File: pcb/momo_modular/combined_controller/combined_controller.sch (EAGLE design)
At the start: 44 parts, among them Q2 P-MOSFET, U1 XRP7659, U2 PIC24FJ64GA306, U3 MCP1702, U5 FLASH8MSOP8, U6 MCP73811

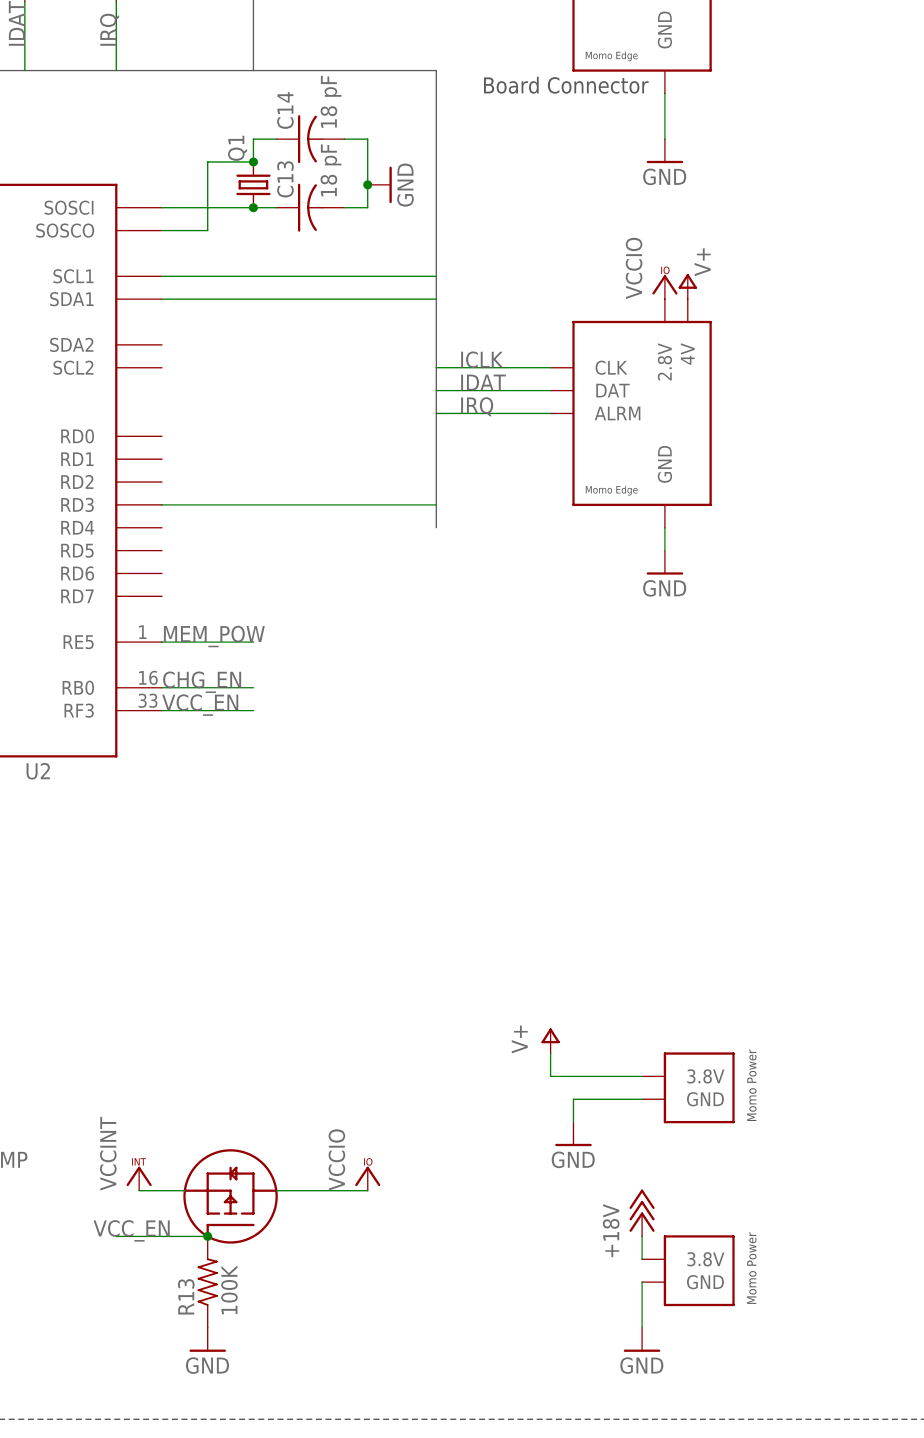
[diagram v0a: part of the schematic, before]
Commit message: Finalize combined controller layout
- Switch power connector to one that doesn't require a board cutout
- Relay out traces better given that we note have more space
- Make the board a regular shape
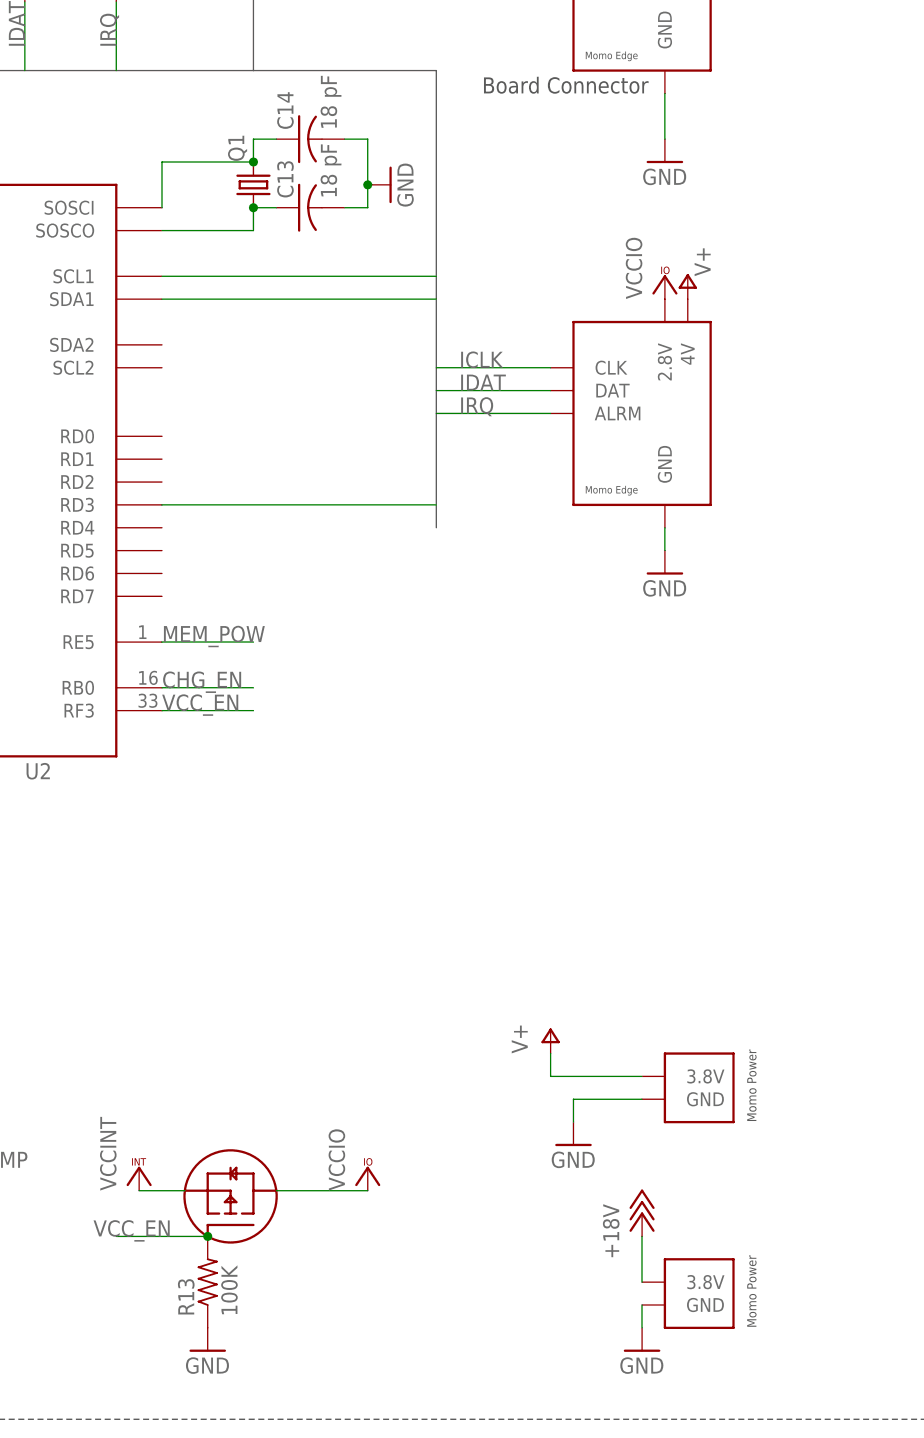
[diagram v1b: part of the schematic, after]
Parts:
- JP4, JP5: value MOMO-EDGE-POWER-M -> MOMO-PWR-HOUSED; device components:MOMO-EDGE-POWER-M -> components:MOMO-PWR-HOUSED; DIGIKEY-PN A19450-ND -> (none)
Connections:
- net +18V: now also JP4.3.8V; no longer JP5.3.8V
- net N$6: now also U2.SOSCI; no longer U2.SOSCO
- net N$7: now also U2.SOSCO; no longer U2.SOSCI
- net V+: now also JP5.3.8V; no longer JP4.3.8V
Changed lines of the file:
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@@
 <?xml version="1.0" encoding="utf-8"?>
 <!DOCTYPE eagle SYSTEM "eagle.dtd">
-<eagle version="6.4">
+<eagle version="6.5.0">
 <drawing>
 <settings>
@@
 <attribute name="DIGIKEY-PN-SOLAR" value="P0.0GCT-ND"/>
 </part>
-<part name="JP5" library="components" deviceset="MOMO-EDGE-POWER-M" device="">
-<attribute name="DIGIKEY-PN" value="A19450-ND"/>
-</part>
-<part name="JP4" library="components" deviceset="MOMO-EDGE-POWER-M" device="">
-<attribute name="DIGIKEY-PN" value="A19450-ND"/>
-</part>
 <part name="VCC2" library="supply1" deviceset="VCCIO" device=""/>
 <part name="VCC11" library="supply1" deviceset="VCCIO" device=""/>
@@
 <attribute name="DIGIKEY-PN" value="445-1265-1-ND"/>
 </part>
+<part name="JP4" library="components" deviceset="MOMO-PWR-HOUSED" device=""/>
+<part name="JP5" library="components" deviceset="MOMO-PWR-HOUSED" device=""/>
 </parts>
 <sheets>
@@
 <attribute name="DIGIKEY-PN-SOLAR" x="-180.34" y="116.84" size="1.778" layer="96" display="off"/>
 </instance>
-<instance part="JP5" gate="G$1" x="-30.48" y="-96.52">
-<attribute name="DIGIKEY-PN" x="-30.48" y="-96.52" size="1.778" layer="96" display="off"/>
-</instance>
-<instance part="JP4" gate="G$1" x="-30.48" y="-76.2">
-<attribute name="DIGIKEY-PN" x="-30.48" y="-76.2" size="1.778" layer="96" display="off"/>
-</instance>
 <instance part="VCC2" gate="G$1" x="-30.48" y="15.24"/>
 <instance part="VCC11" gate="G$1" x="-30.48" y="63.5"/>
@@
 <attribute name="DIGIKEY-PN" x="-205.74" y="68.58" size="1.778" layer="96" display="off"/>
 </instance>
+<instance part="JP4" gate="G$1" x="-30.48" y="-99.06"/>
+<instance part="JP5" gate="G$1" x="-30.48" y="-76.2"/>
 </instances>
 <busses>
@@
 </segment>
 <segment>
-<pinref part="GND7" gate="1" pin="GND"/>
-<pinref part="JP5" gate="G$1" pin="GND"/>
-<wire x1="-33.02" y1="-101.6" x2="-33.02" y2="-96.52" width="0.1524" layer="91"/>
-</segment>
-<segment>
-<pinref part="JP4" gate="G$1" pin="GND"/>
 <pinref part="GND8" gate="1" pin="GND"/>
 <wire x1="-33.02" y1="-76.2" x2="-40.64" y2="-76.2" width="0.1524" layer="91"/>
 <wire x1="-40.64" y1="-76.2" x2="-40.64" y2="-78.74" width="0.1524" layer="91"/>
+<pinref part="JP5" gate="G$1" pin="GND"/>
 </segment>
 <segment>
@@
 <pinref part="GND6" gate="1" pin="GND"/>
 </segment>
+<segment>
+<pinref part="GND7" gate="1" pin="GND"/>
+<wire x1="-33.02" y1="-99.06" x2="-33.02" y2="-101.6" width="0.1524" layer="91"/>
+<pinref part="JP4" gate="G$1" pin="GND"/>
+</segment>
 </net>
 <net name="V+" class="0">
@@
 <wire x1="-33.02" y1="-73.66" x2="-43.18" y2="-73.66" width="0.1524" layer="91"/>
 <wire x1="-43.18" y1="-73.66" x2="-43.18" y2="-71.12" width="0.1524" layer="91"/>
-<pinref part="JP4" gate="G$1" pin="3.8V"/>
+<pinref part="JP5" gate="G$1" pin="3.8V"/>
 </segment>
 </net>
@@
 </segment>
 <segment>
-<pinref part="JP5" gate="G$1" pin="3.8V"/>
 <pinref part="P+5" gate="1" pin="+18V"/>
-<wire x1="-33.02" y1="-93.98" x2="-33.02" y2="-91.44" width="0.1524" layer="91"/>
+<wire x1="-33.02" y1="-96.52" x2="-33.02" y2="-91.44" width="0.1524" layer="91"/>
+<pinref part="JP4" gate="G$1" pin="3.8V"/>
 </segment>
 </net>
@@
 <wire x1="-76.2" y1="27.94" x2="-76.2" y2="30.48" width="0.1524" layer="91"/>
 <wire x1="-76.2" y1="30.48" x2="-73.66" y2="30.48" width="0.1524" layer="91"/>
-<pinref part="U2" gate="G$1" pin="SOSCO"/>
-<wire x1="-86.36" y1="20.32" x2="-81.28" y2="20.32" width="0.1524" layer="91"/>
-<wire x1="-81.28" y1="20.32" x2="-81.28" y2="27.94" width="0.1524" layer="91"/>
-<wire x1="-81.28" y1="27.94" x2="-76.2" y2="27.94" width="0.1524" layer="91"/>
 <junction x="-76.2" y="27.94"/>
+<pinref part="U2" gate="G$1" pin="SOSCI"/>
+<wire x1="-86.36" y1="22.86" x2="-86.36" y2="27.94" width="0.1524" layer="91"/>
+<wire x1="-86.36" y1="27.94" x2="-76.2" y2="27.94" width="0.1524" layer="91"/>
 </segment>
 </net>
@@
 <pinref part="C13" gate="G$1" pin="1"/>
 <wire x1="-73.66" y1="22.86" x2="-76.2" y2="22.86" width="0.1524" layer="91"/>
-<pinref part="U2" gate="G$1" pin="SOSCI"/>
-<wire x1="-86.36" y1="22.86" x2="-76.2" y2="22.86" width="0.1524" layer="91"/>
+<wire x1="-76.2" y1="22.86" x2="-76.2" y2="20.32" width="0.1524" layer="91"/>
 <junction x="-76.2" y="22.86"/>
-</segment>
-</net>
+<pinref part="U2" gate="G$1" pin="SOSCO"/>
+<wire x1="-76.2" y1="20.32" x2="-86.36" y2="20.32" width="0.1524" layer="91"/>
+</segment>
+</net>

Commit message: Final review of combined controller
- checked footprint of uc
- added bypass for battery if required
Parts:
- added R12: 0R, rcl:R-US_R0603
- C15: DIGIKEY-PN 1276-1119-1-ND -> 1276-2893-1-ND
- JP3: POPULATE (none) -> no
- Q1: value (none) -> 32.768khz
- Q2: DESCRIPTION (none) -> P Channel MOSFET
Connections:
- net VBAT: now also R12.2
- net VCCINT: now also R12.1
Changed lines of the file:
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@@
 <part name="VCC2" library="supply1" deviceset="VCCIO" device=""/>
 <part name="VCC11" library="supply1" deviceset="VCCIO" device=""/>
-<part name="Q2" library="components" deviceset="P-MOSFET" device=""/>
+<part name="Q2" library="components" deviceset="P-MOSFET" device="">
+<attribute name="DESCRIPTION" value="P Channel MOSFET"/>
+</part>
 <part name="R13" library="rcl" deviceset="R-US_" device="R0603" value="100K">
 <attribute name="DIGIKEY-PN" value="P100KHCT-ND"/>
@@
 <attribute name="DIGIKEY-PN" value="S1011EC-06-ND"/>
 </part>
-<part name="JP3" library="pinhead" deviceset="PINHD-1X1" device=""/>
+<part name="JP3" library="pinhead" deviceset="PINHD-1X1" device="">
+<attribute name="DIGIKEY-PN" value=""/>
+<attribute name="POPULATE" value="no"/>
+</part>
 <part name="D2" library="diode" deviceset="DIODE-" device="DO214AC">
 <attribute name="DESCRIPTION" value="Schottky Diode "/>
@@
 <attribute name="DIGIKEY-PN-SOLAR" value="MCP73811T-420I/OTCT-ND"/>
 </part>
-<part name="Q1" library="crystal" deviceset="CRYSTAL" device="TC26H">
+<part name="Q1" library="crystal" deviceset="CRYSTAL" device="TC26H" value="32.768khz">
 <attribute name="DIGIKEY-PN" value="535-9034-ND"/>
 </part>
@@
 <part name="GND5" library="supply1" deviceset="GND" device=""/>
 <part name="C15" library="rcl" deviceset="C-US" device="C0805" value="10 uF">
-<attribute name="DIGIKEY-PN" value="1276-1119-1-ND"/>
+<attribute name="DIGIKEY-PN" value="1276-2893-1-ND"/>
 </part>
 <part name="GND6" library="supply1" deviceset="GND" device=""/>
@@
 <part name="JP4" library="components" deviceset="MOMO-PWR-HOUSED" device=""/>
 <part name="JP5" library="components" deviceset="MOMO-PWR-HOUSED" device=""/>
+<part name="R12" library="rcl" deviceset="R-US_" device="R0603" value="0R">
+<attribute name="DIGIKEY-PN" value="P0.0GCT-ND"/>
+<attribute name="POPULATE" value="no"/>
+</part>
+<part name="VCC12" library="supply1" deviceset="VCCINT" device=""/>
 </parts>
 <sheets>
 <sheet>
 <plain>
-<wire x1="-226.06" y1="127" x2="-226.06" y2="-111.76" width="0.1524" layer="97" style="longdash"/>
-<wire x1="-226.06" y1="-111.76" x2="10.16" y2="-111.76" width="0.1524" layer="97" style="longdash"/>
+<wire x1="-238.76" y1="127" x2="-238.76" y2="-111.76" width="0.1524" layer="97" style="longdash"/>
+<wire x1="-238.76" y1="-111.76" x2="10.16" y2="-111.76" width="0.1524" layer="97" style="longdash"/>
 <wire x1="10.16" y1="-111.76" x2="10.16" y2="127" width="0.1524" layer="97" style="longdash"/>
-<wire x1="10.16" y1="127" x2="-226.06" y2="127" width="0.1524" layer="97" style="longdash"/>
+<wire x1="10.16" y1="127" x2="-238.76" y2="127" width="0.1524" layer="97" style="longdash"/>
 <wire x1="-223.52" y1="-109.22" x2="-223.52" y2="-96.52" width="0.3048" layer="97"/>
 <wire x1="-223.52" y1="-96.52" x2="-223.52" y2="-91.44" width="0.3048" layer="97"/>
@@
 <instance part="VCC2" gate="G$1" x="-30.48" y="15.24"/>
 <instance part="VCC11" gate="G$1" x="-30.48" y="63.5"/>
-<instance part="Q2" gate="G$1" x="-78.74" y="-86.36" rot="R90"/>
+<instance part="Q2" gate="G$1" x="-78.74" y="-86.36" rot="R90">
+<attribute name="DESCRIPTION" x="-78.74" y="-86.36" size="1.778" layer="96" rot="R90" display="off"/>
+</instance>
 <instance part="R13" gate="G$1" x="-81.28" y="-96.52" rot="R90">
 <attribute name="DIGIKEY-PN" x="-81.28" y="-96.52" size="1.778" layer="96" rot="R90" display="off"/>
@@
 <attribute name="DIGIKEY-PN" x="-35.56" y="-7.62" size="1.778" layer="96" display="off"/>
 </instance>
-<instance part="JP3" gate="G$1" x="-160.02" y="50.8"/>
+<instance part="JP3" gate="G$1" x="-160.02" y="50.8">
+<attribute name="DIGIKEY-PN" x="-160.02" y="50.8" size="1.778" layer="96" display="off"/>
+<attribute name="POPULATE" x="-160.02" y="50.8" size="1.778" layer="96" display="off"/>
+</instance>
 <instance part="D2" gate="G$1" x="-215.9" y="104.14">
 <attribute name="DIGIKEY-PN" x="-215.9" y="104.14" size="1.778" layer="96" display="off"/>
@@
 <instance part="JP4" gate="G$1" x="-30.48" y="-99.06"/>
 <instance part="JP5" gate="G$1" x="-30.48" y="-76.2"/>
+<instance part="R12" gate="G$1" x="-231.14" y="76.2" rot="R270">
+<attribute name="POPULATE" x="-231.14" y="76.2" size="1.778" layer="96" rot="R270" display="off"/>
+<attribute name="DIGIKEY-PN" x="-231.14" y="76.2" size="1.778" layer="96" rot="R270" display="off"/>
+</instance>
+<instance part="VCC12" gate="G$1" x="-231.14" y="83.82"/>
 </instances>
 <busses>
 <bus name="SPI:CS,SDI,SDO,SCLK">
 <segment>
-<wire x1="-200.66" y1="2.54" x2="-200.66" y2="-63.5" width="0.762" layer="92"/>
+<wire x1="-200.66" y1="-22.86" x2="-200.66" y2="-63.5" width="0.762" layer="92"/>
 </segment>
 </bus>
@@
 <junction x="-198.12" y="71.12"/>
 </segment>
+<segment>
+<pinref part="R12" gate="G$1" pin="1"/>
+<pinref part="VCC12" gate="G$1" pin="VCCINT"/>
+</segment>
 </net>
 <net name="CS" class="0">
@@
 <wire x1="-213.36" y1="71.12" x2="-220.98" y2="71.12" width="0.1524" layer="91"/>
 <junction x="-220.98" y="71.12"/>
-</segment>
-</net>
+<pinref part="R12" gate="G$1" pin="2"/>
+<wire x1="-220.98" y1="71.12" x2="-231.14" y2="71.12" width="0.1524" layer="91"/>
+</segment>
+</net>
